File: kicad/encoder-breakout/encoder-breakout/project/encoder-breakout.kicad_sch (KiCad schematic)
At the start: 8 parts, among them J1 Conn_01x05_Socket, SW1 RotaryEncoder_Switch

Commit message: Final updates for manufacturing
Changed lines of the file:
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@@
 (kicad_sch (version 20230121) (generator eeschema)
   (paper "A4")
+  (junction (at 177.8 81.28) (diameter 0) (color 0 0 0 0)
+  )
   (junction (at 125.73 72.39) (diameter 0) (color 0 0 0 0)
   )
   (junction (at 138.43 90.17) (diameter 0) (color 0 0 0 0)
+  )
+  (junction (at 177.8 93.98) (diameter 0) (color 0 0 0 0)
   )
   (junction (at 55.88 85.09) (diameter 0) (color 0 0 0 0)
@@
     )
   )
+  (symbol (lib_id "power:PWR_FLAG") (at 177.8 93.98 180) (unit 1)
+    (in_bom yes) (on_board yes) (dnp no) (fields_autoplaced)
+    (property "Reference" "#FLG01" (at 177.8 95.885 0)
+      (effects (font (size 1.27 1.27)) hide)
+    )
+    (property "Value" "PWR_FLAG" (at 177.8 99.06 0)
+      (effects (font (size 1.27 1.27)))
+    )
+    (property "Footprint" "" (at 177.8 93.98 0)
+      (effects (font (size 1.27 1.27)) hide)
+    )
+    (property "Datasheet" "~" (at 177.8 93.98 0)
+      (effects (font (size 1.27 1.27)) hide)
+    )
+    (pin "1")
+    (instances
+      (project "encoder-breakout"
+        (path "/055254a7-bdb7-4164-9be8-bc660cab8db9"
+          (reference "#FLG01") (unit 1)
+        )
+      )
+    )
+  )
   (symbol (lib_id "power:GND") (at 125.73 80.01 0) (unit 1)
     (in_bom yes) (on_board yes) (dnp no) (fields_autoplaced)
@@
         )
       )
+    )
+  )
+  (symbol (lib_id "power:PWR_FLAG") (at 177.8 81.28 0) (unit 1)
+    (in_bom yes) (on_board yes) (dnp no) (fields_autoplaced)
+    (property "Reference" "#FLG02" (at 177.8 79.375 0)
+      (effects (font (size 1.27 1.27)) hide)
+    )
+    (property "Value" "PWR_FLAG" (at 177.8 76.2 0)
+      (effects (font (size 1.27 1.27)))
+    )
+    (property "Footprint" "" (at 177.8 81.28 0)
+      (effects (font (size 1.27 1.27)) hide)
+    )
+    (property "Datasheet" "~" (at 177.8 81.28 0)
+      (effects (font (size 1.27 1.27)) hide)
+    )
+    (pin "1")
+    (instances
+      (project "encoder-breakout"
+        (path "/055254a7-bdb7-4164-9be8-bc660cab8db9"
+          (reference "#FLG02") (unit 1)
+        )
+      )

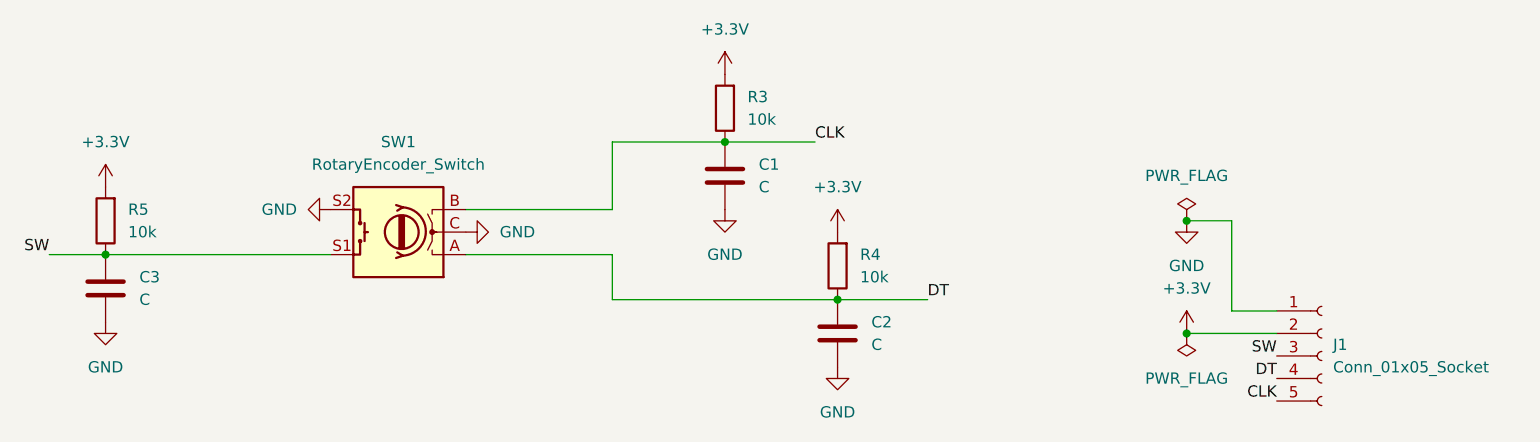
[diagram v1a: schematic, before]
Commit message: Changes after manufacting
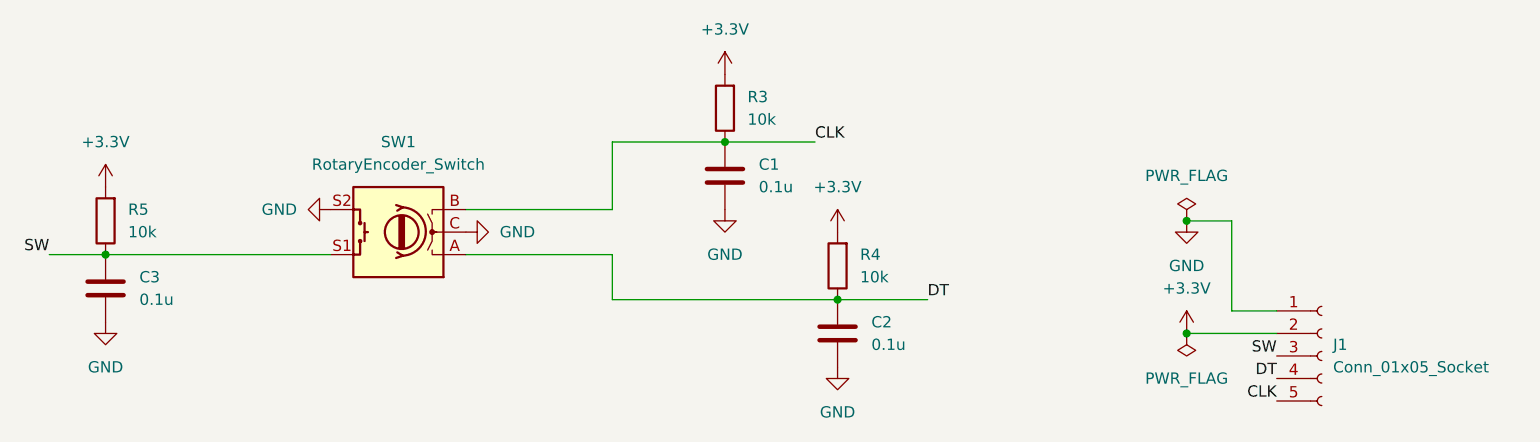
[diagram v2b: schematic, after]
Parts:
- C1, C2, C3: value C -> 0.1u
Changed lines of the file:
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@@
       (effects (font (size 1.27 1.27)) (justify left))
     )
-    (property "Value" "C" (at 142.24 95.25 0)
+    (property "Value" "0.1u" (at 142.24 95.25 0)
       (effects (font (size 1.27 1.27)) (justify left))
     )
@@
       (effects (font (size 1.27 1.27)) (justify left))
     )
-    (property "Value" "C" (at 59.69 90.17 0)
+    (property "Value" "0.1u" (at 59.69 90.17 0)
       (effects (font (size 1.27 1.27)) (justify left))
     )
@@
       (effects (font (size 1.27 1.27)) (justify left))
     )
-    (property "Value" "C" (at 129.54 77.47 0)
+    (property "Value" "0.1u" (at 129.54 77.47 0)
       (effects (font (size 1.27 1.27)) (justify left))
     )
